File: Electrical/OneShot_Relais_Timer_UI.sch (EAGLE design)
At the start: 13 parts, among them IC1 4511D

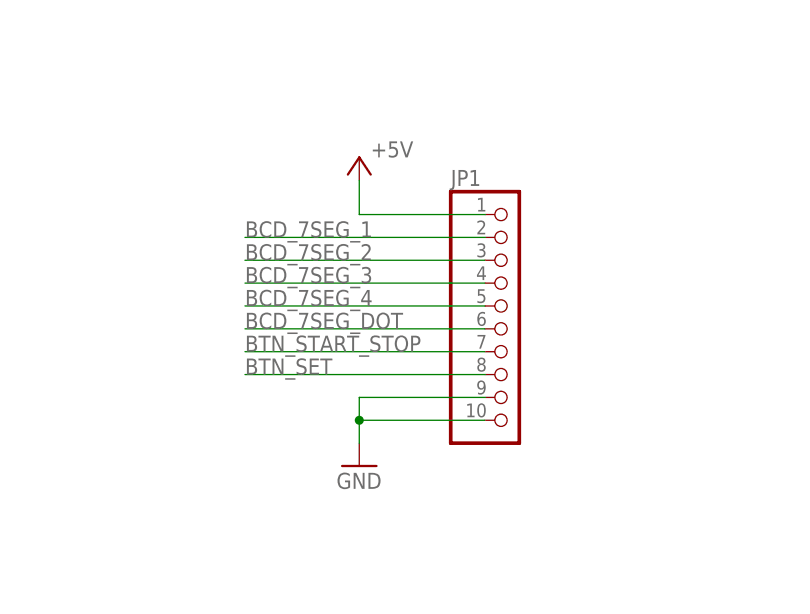
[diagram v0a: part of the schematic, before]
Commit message: Added mounting holes to PCB, moved relay, small adaptions to UI PCB
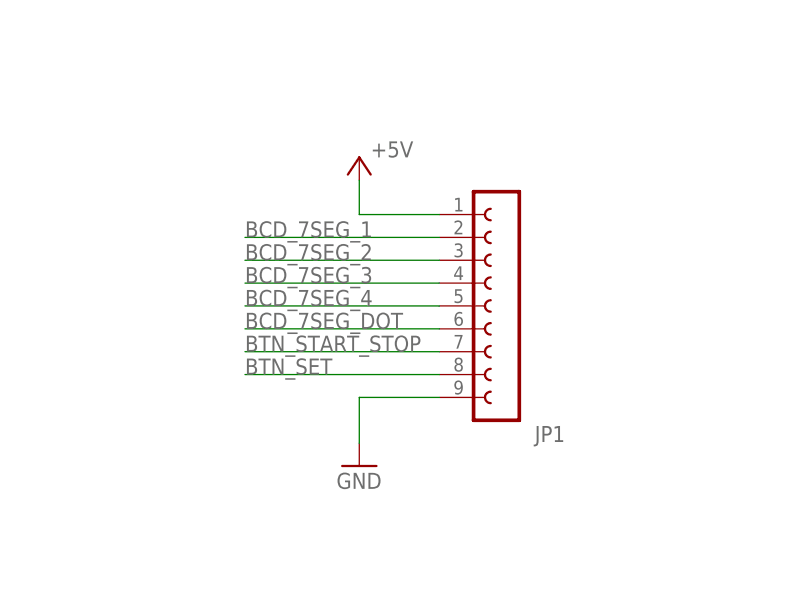
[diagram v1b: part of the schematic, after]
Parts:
- JP1: device pinhead:PINHD-1X10 -> OwnDevices:FE09-1
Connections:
- net GND: no longer JP1.10
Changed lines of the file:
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@@
 <part name="S2" library="OwnDevices" library_urn="urn:adsk.eagle:library:19498084" deviceset="KURZHUBTASTER" device="" package3d_urn="urn:adsk.eagle:package:21817514/2" value="START/STOP"/>
 <part name="GND5" library="supply1" library_urn="urn:adsk.eagle:library:371" deviceset="GND" device=""/>
-<part name="JP1" library="pinhead" library_urn="urn:adsk.eagle:library:325" deviceset="PINHD-1X10" device="" package3d_urn="urn:adsk.eagle:package:22406/2"/>
+<part name="JP1" library="OwnDevices" library_urn="urn:adsk.eagle:library:19498084" deviceset="FE09-1" device="" package3d_urn="urn:adsk.eagle:package:37698325/2"/>
 <part name="P+1" library="supply1" library_urn="urn:adsk.eagle:library:371" deviceset="+5V" device=""/>
 <part name="GND1" library="supply1" library_urn="urn:adsk.eagle:library:371" deviceset="GND" device=""/>
@@
 <attribute name="VALUE" x="53.34" y="96.52" size="1.778" layer="96"/>
 </instance>
-<instance part="JP1" gate="A" x="198.12" y="115.57" smashed="yes">
-<attribute name="NAME" x="191.77" y="128.905" size="1.778" layer="95"/>
-<attribute name="VALUE" x="191.77" y="97.79" size="1.778" layer="96"/>
+<instance part="JP1" gate="G$1" x="198.12" y="115.57" smashed="yes" rot="R180">
+<attribute name="NAME" x="204.47" y="102.235" size="1.778" layer="95" rot="R180"/>
+<attribute name="VALUE" x="204.47" y="133.35" size="1.778" layer="96" rot="R180"/>
 </instance>
 <instance part="P+1" gate="1" x="181.61" y="132.08" smashed="yes">
@@
 </segment>
 <segment>
-<pinref part="JP1" gate="A" pin="9"/>
+<pinref part="JP1" gate="G$1" pin="9"/>
 <pinref part="GND1" gate="1" pin="GND"/>
-<wire x1="195.58" y1="105.41" x2="181.61" y2="105.41" width="0.1524" layer="91"/>
-<wire x1="181.61" y1="105.41" x2="181.61" y2="102.87" width="0.1524" layer="91"/>
-<pinref part="JP1" gate="A" pin="10"/>
-<wire x1="181.61" y1="102.87" x2="181.61" y2="100.33" width="0.1524" layer="91"/>
-<wire x1="195.58" y1="102.87" x2="181.61" y2="102.87" width="0.1524" layer="91"/>
-<junction x="181.61" y="102.87"/>
+<wire x1="190.5" y1="105.41" x2="181.61" y2="105.41" width="0.1524" layer="91"/>
+<wire x1="181.61" y1="105.41" x2="181.61" y2="100.33" width="0.1524" layer="91"/>
 </segment>
 </net>
@@
 </segment>
 <segment>
-<pinref part="JP1" gate="A" pin="2"/>
-<wire x1="195.58" y1="123.19" x2="168.91" y2="123.19" width="0.1524" layer="91"/>
+<pinref part="JP1" gate="G$1" pin="2"/>
+<wire x1="190.5" y1="123.19" x2="168.91" y2="123.19" width="0.1524" layer="91"/>
 <label x="168.91" y="123.19" size="1.778" layer="95"/>
 </segment>
@@
 </segment>
 <segment>
-<pinref part="JP1" gate="A" pin="5"/>
-<wire x1="195.58" y1="115.57" x2="168.91" y2="115.57" width="0.1524" layer="91"/>
+<pinref part="JP1" gate="G$1" pin="5"/>
+<wire x1="190.5" y1="115.57" x2="168.91" y2="115.57" width="0.1524" layer="91"/>
 <label x="168.91" y="115.57" size="1.778" layer="95"/>
 </segment>
@@
 </segment>
 <segment>
-<pinref part="JP1" gate="A" pin="4"/>
-<wire x1="195.58" y1="118.11" x2="168.91" y2="118.11" width="0.1524" layer="91"/>
+<pinref part="JP1" gate="G$1" pin="4"/>
+<wire x1="190.5" y1="118.11" x2="168.91" y2="118.11" width="0.1524" layer="91"/>
 <label x="168.91" y="118.11" size="1.778" layer="95"/>
 </segment>
@@
 </segment>
 <segment>
-<pinref part="JP1" gate="A" pin="3"/>
-<wire x1="195.58" y1="120.65" x2="168.91" y2="120.65" width="0.1524" layer="91"/>
+<pinref part="JP1" gate="G$1" pin="3"/>
+<wire x1="190.5" y1="120.65" x2="168.91" y2="120.65" width="0.1524" layer="91"/>
 <label x="168.91" y="120.65" size="1.778" layer="95"/>
 </segment>
@@
 </segment>
 <segment>
-<pinref part="JP1" gate="A" pin="1"/>
+<pinref part="JP1" gate="G$1" pin="1"/>
 <pinref part="P+1" gate="1" pin="+5V"/>
-<wire x1="195.58" y1="125.73" x2="181.61" y2="125.73" width="0.1524" layer="91"/>
+<wire x1="190.5" y1="125.73" x2="181.61" y2="125.73" width="0.1524" layer="91"/>
 <wire x1="181.61" y1="125.73" x2="181.61" y2="129.54" width="0.1524" layer="91"/>
 </segment>
@@
 </segment>
 <segment>
-<pinref part="JP1" gate="A" pin="6"/>
-<wire x1="195.58" y1="113.03" x2="168.91" y2="113.03" width="0.1524" layer="91"/>
+<pinref part="JP1" gate="G$1" pin="6"/>
+<wire x1="190.5" y1="113.03" x2="168.91" y2="113.03" width="0.1524" layer="91"/>
 <label x="168.91" y="113.03" size="1.778" layer="95"/>
 </segment>
@@
 </segment>
 <segment>
-<pinref part="JP1" gate="A" pin="7"/>
-<wire x1="195.58" y1="110.49" x2="168.91" y2="110.49" width="0.1524" layer="91"/>
+<pinref part="JP1" gate="G$1" pin="7"/>
+<wire x1="190.5" y1="110.49" x2="168.91" y2="110.49" width="0.1524" layer="91"/>
 <label x="168.91" y="110.49" size="1.778" layer="95"/>
 </segment>
@@
 </segment>
 <segment>
-<pinref part="JP1" gate="A" pin="8"/>
-<wire x1="195.58" y1="107.95" x2="168.91" y2="107.95" width="0.1524" layer="91"/>
+<pinref part="JP1" gate="G$1" pin="8"/>
+<wire x1="190.5" y1="107.95" x2="168.91" y2="107.95" width="0.1524" layer="91"/>
 <label x="168.91" y="107.95" size="1.778" layer="95"/>
 </segment>

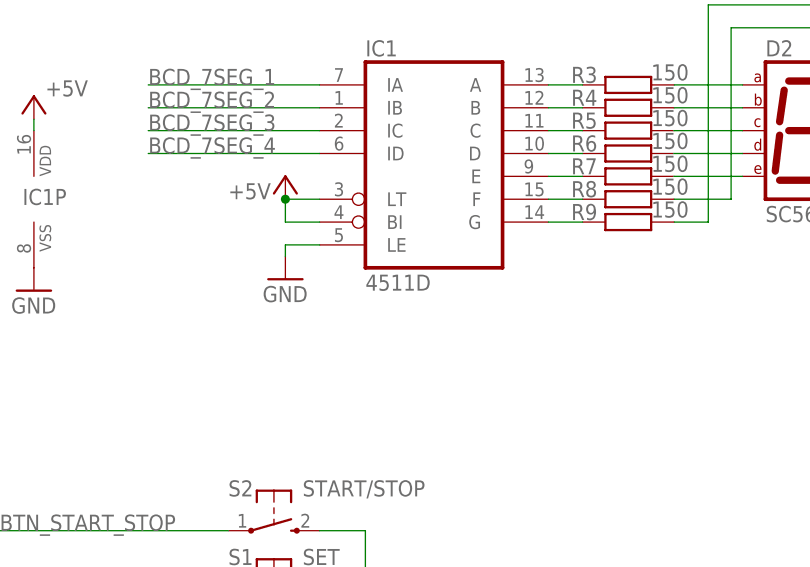
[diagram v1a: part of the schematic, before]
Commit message: Replaced BCD 7Segment IC with correct type (footprint), corrected routing of UI PCB
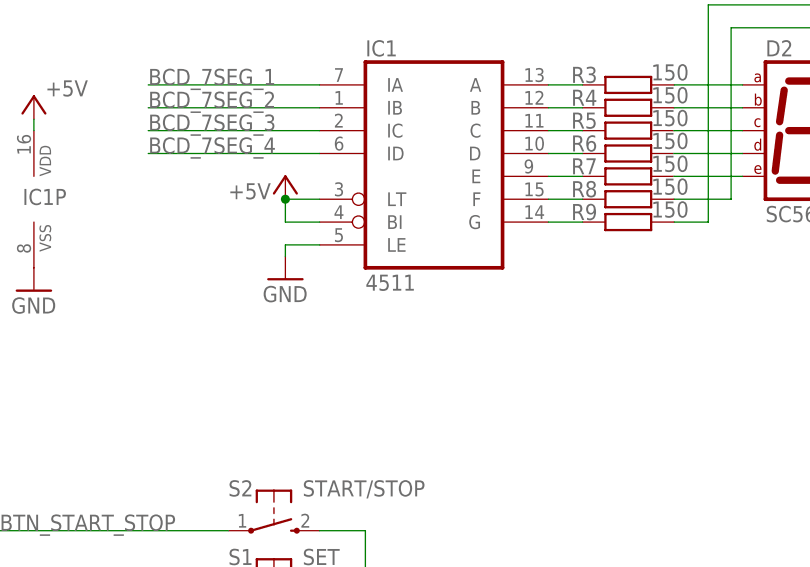
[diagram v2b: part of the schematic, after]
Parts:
- IC1: value 4511D -> 4511; device 45xx:4511D -> OwnDevices:4511
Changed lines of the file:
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@@
 <drawing>
 <settings>
-<setting alwaysvectorfont="no"/>
+<setting alwaysvectorfont="yes"/>
 <setting verticaltext="up"/>
 </settings>
@@
 <part name="R8" library="OwnDevices" library_urn="urn:adsk.eagle:library:19498084" deviceset="R-EU_" device="R0805" package3d_urn="urn:adsk.eagle:package:23553/2" value="150"/>
 <part name="R9" library="OwnDevices" library_urn="urn:adsk.eagle:library:19498084" deviceset="R-EU_" device="R0805" package3d_urn="urn:adsk.eagle:package:23553/2" value="150"/>
-<part name="IC1" library="45xx" library_urn="urn:adsk.eagle:library:82" deviceset="4511" device="D" package3d_urn="urn:adsk.eagle:package:1005/2"/>
+<part name="IC1" library="OwnDevices" library_urn="urn:adsk.eagle:library:19498084" deviceset="4511" device="" package3d_urn="urn:adsk.eagle:package:37818661/1"/>
 <part name="P+4" library="supply1" library_urn="urn:adsk.eagle:library:371" deviceset="+5V" device=""/>
 <part name="GND3" library="supply1" library_urn="urn:adsk.eagle:library:371" deviceset="GND" device=""/>

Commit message: Small adaptions to PCBs, schematics, and mechanical components
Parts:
- R10, R3, R4, R5, R6, R7, R8, R9: value 150 -> 330
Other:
- note added: "7 Segment Display"
- note added: "Buttons"
- note added: "Connector to Main PCB"
- note added: "HW_v1"
- note removed: "7 Segment Anzeige richtig?"
- moved on the sheet: D2, IC1, IC1P, JP1, R10, R3, R4, R5, R6, R7, R8, R9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
